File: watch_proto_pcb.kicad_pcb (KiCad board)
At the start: 2 copper layers, 32 parts, among them P1 CONN_01X04, P2 CONN_01X06, P3 CONN_01X04, Q1 RZM001P02, Q2 RZM001P02, Q3 RZM001P02, Q4 RZM001P02, U1 TLC5954

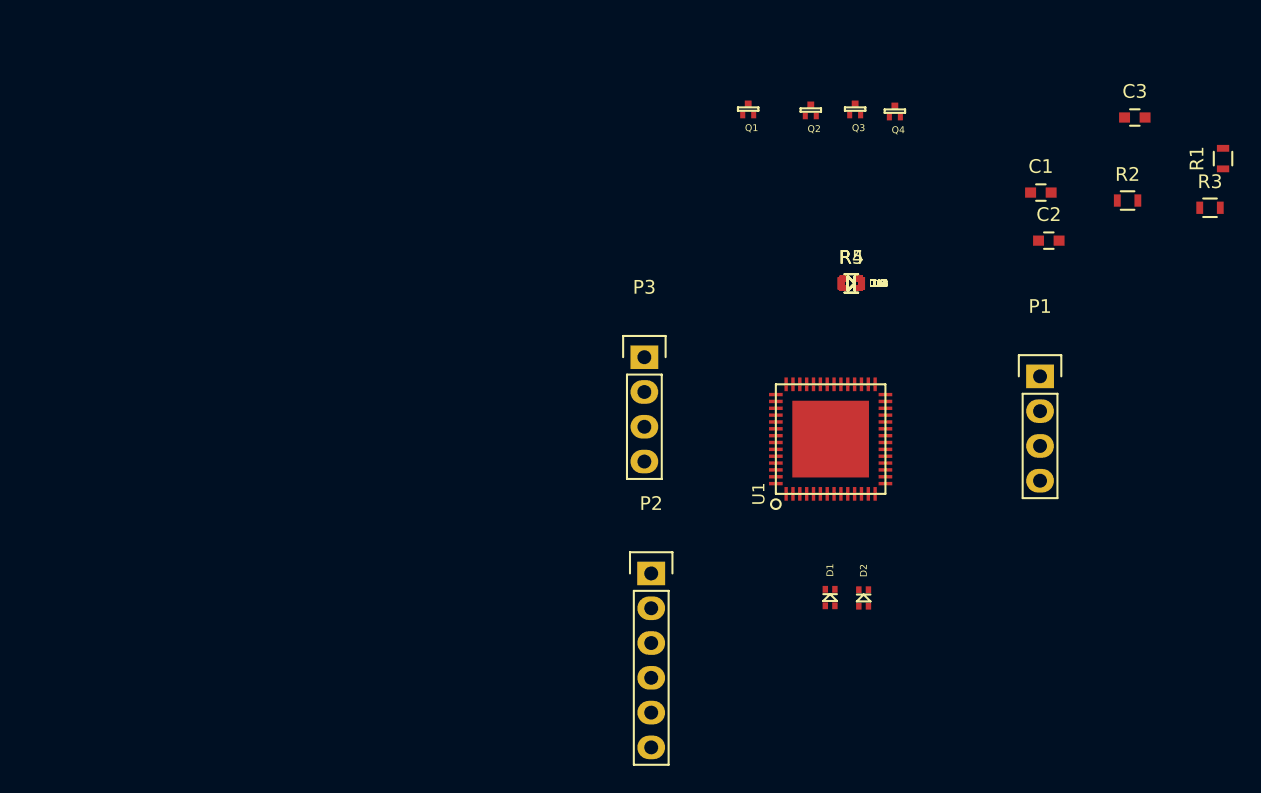
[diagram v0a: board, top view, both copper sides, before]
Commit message: Added debug messages and changed UI for rotation angle
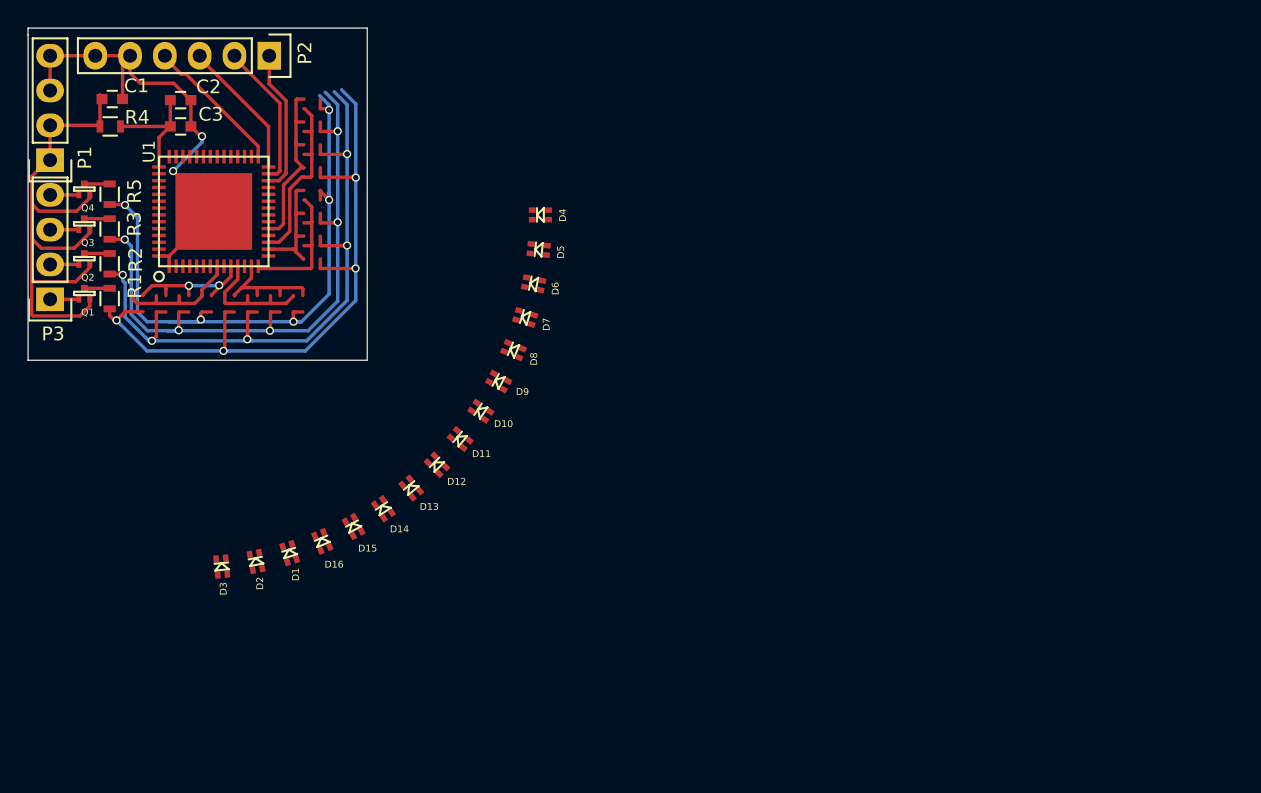
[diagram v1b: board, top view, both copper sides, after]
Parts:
- moved R1 81.9 mm to (94.3, 106.1), turned to 270 degrees
- moved R3 80.4 mm to (94.3, 101.0), turned to 270 degrees
- moved R2 74.5 mm to (94.3, 103.6), turned to 270 degrees
- moved P1 74.0 mm to (90.0, 96.0), turned to 180 degrees
- moved C3 69.7 mm to (99.5, 93.5)
- moved C1 68.1 mm to (94.5, 91.5)
- moved C2 64.2 mm to (99.5, 91.6)
- moved Q4 59.5 mm to (92.5, 97.7)
- moved Q3 56.9 mm to (92.5, 100.3)
- moved R4 55.3 mm to (94.4, 93.5), turned to 180 degrees
- moved R5 54.5 mm to (94.3, 98.5), turned to 270 degrees
- moved Q2 54.1 mm to (92.5, 102.8)
- moved D3 50.4 mm to (102.5, 125.7), turned to 95.625 degrees
- moved Q1 50.3 mm to (92.5, 105.4)
- moved U1 48.0 mm to (102.0, 99.8)
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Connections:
- C1 pad 1: /proto_TLC/TLC_PWR -> VDD
- C3 pad 1: VDD -> /proto_TLC/TLC_PWR
- D10 pad 1: /proto_TLC/B1 -> /proto_TLC/B2
- D10 pad 2: /proto_TLC/LED_PWR_OUT_0 -> /proto_TLC/LED_PWR_OUT_1
- D10 pad 3: /proto_TLC/R1 -> /proto_TLC/R2
- D10 pad 4: /proto_TLC/LED_PWR_OUT_0 -> /proto_TLC/LED_PWR_OUT_1
- D11 pad 1: /proto_TLC/B3 -> /proto_TLC/B2
- D11 pad 2: /proto_TLC/LED_PWR_OUT_1 -> /proto_TLC/LED_PWR_OUT_2
- D11 pad 3: /proto_TLC/R3 -> /proto_TLC/R2
- D11 pad 4: /proto_TLC/LED_PWR_OUT_1 -> /proto_TLC/LED_PWR_OUT_2
- D12 pad 1: /proto_TLC/B1 -> /proto_TLC/B2
- D12 pad 2: /proto_TLC/LED_PWR_OUT_1 -> /proto_TLC/LED_PWR_OUT_3
- D12 pad 3: /proto_TLC/R1 -> /proto_TLC/R2
- D12 pad 4: /proto_TLC/LED_PWR_OUT_1 -> /proto_TLC/LED_PWR_OUT_3
- D13 pad 2: /proto_TLC/LED_PWR_OUT_2 -> /proto_TLC/LED_PWR_OUT_0
- D13 pad 4: /proto_TLC/LED_PWR_OUT_2 -> /proto_TLC/LED_PWR_OUT_0
- D14 pad 1: /proto_TLC/B1 -> /proto_TLC/B3
- D14 pad 2: /proto_TLC/LED_PWR_OUT_2 -> /proto_TLC/LED_PWR_OUT_1
- D14 pad 3: /proto_TLC/R1 -> /proto_TLC/R3
- D14 pad 4: /proto_TLC/LED_PWR_OUT_2 -> /proto_TLC/LED_PWR_OUT_1
- D15 pad 2: /proto_TLC/LED_PWR_OUT_3 -> /proto_TLC/LED_PWR_OUT_2
- D15 pad 4: /proto_TLC/LED_PWR_OUT_3 -> /proto_TLC/LED_PWR_OUT_2
- D16 pad 1: /proto_TLC/B1 -> /proto_TLC/B3
- D16 pad 3: /proto_TLC/R1 -> /proto_TLC/R3
- D2 pad 1: /proto_TLC/B2 -> /proto_TLC/B0
- D2 pad 2: /proto_TLC/LED_PWR_OUT_0 -> /proto_TLC/LED_PWR_OUT_1
- D2 pad 3: /proto_TLC/R2 -> /proto_TLC/R0
- D2 pad 4: /proto_TLC/LED_PWR_OUT_0 -> /proto_TLC/LED_PWR_OUT_1
- D3 pad 2: /proto_TLC/LED_PWR_OUT_1 -> /proto_TLC/LED_PWR_OUT_2
- D3 pad 4: /proto_TLC/LED_PWR_OUT_1 -> /proto_TLC/LED_PWR_OUT_2
- D4 pad 1: /proto_TLC/B2 -> /proto_TLC/B0
- D4 pad 2: /proto_TLC/LED_PWR_OUT_1 -> /proto_TLC/LED_PWR_OUT_3
- D4 pad 3: /proto_TLC/R2 -> /proto_TLC/R0
- D4 pad 4: /proto_TLC/LED_PWR_OUT_1 -> /proto_TLC/LED_PWR_OUT_3
- D5 pad 1: /proto_TLC/B0 -> /proto_TLC/B1
- D5 pad 2: /proto_TLC/LED_PWR_OUT_2 -> /proto_TLC/LED_PWR_OUT_0
- D5 pad 3: /proto_TLC/R0 -> /proto_TLC/R1
- D5 pad 4: /proto_TLC/LED_PWR_OUT_2 -> /proto_TLC/LED_PWR_OUT_0
- D6 pad 1: /proto_TLC/B2 -> /proto_TLC/B1
- D6 pad 2: /proto_TLC/LED_PWR_OUT_2 -> /proto_TLC/LED_PWR_OUT_1
- D6 pad 3: /proto_TLC/R2 -> /proto_TLC/R1
- D6 pad 4: /proto_TLC/LED_PWR_OUT_2 -> /proto_TLC/LED_PWR_OUT_1
- D7 pad 1: /proto_TLC/B0 -> /proto_TLC/B1
- D7 pad 2: /proto_TLC/LED_PWR_OUT_3 -> /proto_TLC/LED_PWR_OUT_2
- D7 pad 3: /proto_TLC/R0 -> /proto_TLC/R1
- D7 pad 4: /proto_TLC/LED_PWR_OUT_3 -> /proto_TLC/LED_PWR_OUT_2
- D8 pad 1: /proto_TLC/B2 -> /proto_TLC/B1
- D8 pad 3: /proto_TLC/R2 -> /proto_TLC/R1
- D9 pad 1: /proto_TLC/B3 -> /proto_TLC/B2
- D9 pad 3: /proto_TLC/R3 -> Net-(D9-Pad3)
- R4 pad 1: /proto_TLC/LED_MOS_3 -> /proto_TLC/TLC_PWR
- R4 pad 2: /proto_TLC/LED_PWR_OUT_3 -> VDD
- R5 pad 1: /proto_TLC/TLC_PWR -> /proto_TLC/LED_MOS_3
- R5 pad 2: VDD -> /proto_TLC/LED_PWR_OUT_3
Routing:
- net /proto_TLC/LED_PWR_OUT_1: track 0.00 -> 49.4 mm, vias 0 -> 5
- net /proto_TLC/LED_PWR_OUT_3: track 0.00 -> 48.4 mm, vias 0 -> 5
- net /proto_TLC/LED_PWR_OUT_2: track 0.00 -> 47.8 mm, vias 0 -> 5
- net /proto_TLC/LED_PWR_OUT_0: track 0.00 -> 46.0 mm, vias 0 -> 3
- net VDD: track 0.00 -> 42.5 mm
- net GND: track 0.00 -> 35.0 mm, vias 0 -> 2
- net /proto_TLC/R3: track 0.00 -> 13.4 mm
- net /proto_TLC/B3: track 0.00 -> 13.2 mm
- net /proto_TLC/LAT: track 0.00 -> 10.7 mm
- net /proto_TLC/SIN: track 0.00 -> 10.6 mm
- net /proto_TLC/BLANK: track 0.00 -> 10.4 mm
- net /proto_TLC/R2: track 0.00 -> 10.4 mm
- net /proto_TLC/SCLK: track 0.00 -> 10.2 mm
- net /proto_TLC/B0: track 0.00 -> 10.2 mm, vias 0 -> 2
- net /proto_TLC/R1: track 0.00 -> 9.57 mm
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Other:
- board outline added: 24.8 x 24.3 mm
- net class small added: clearance 0.2, trace_width 0.2032, via_dia 7.62, via_drill 3.81

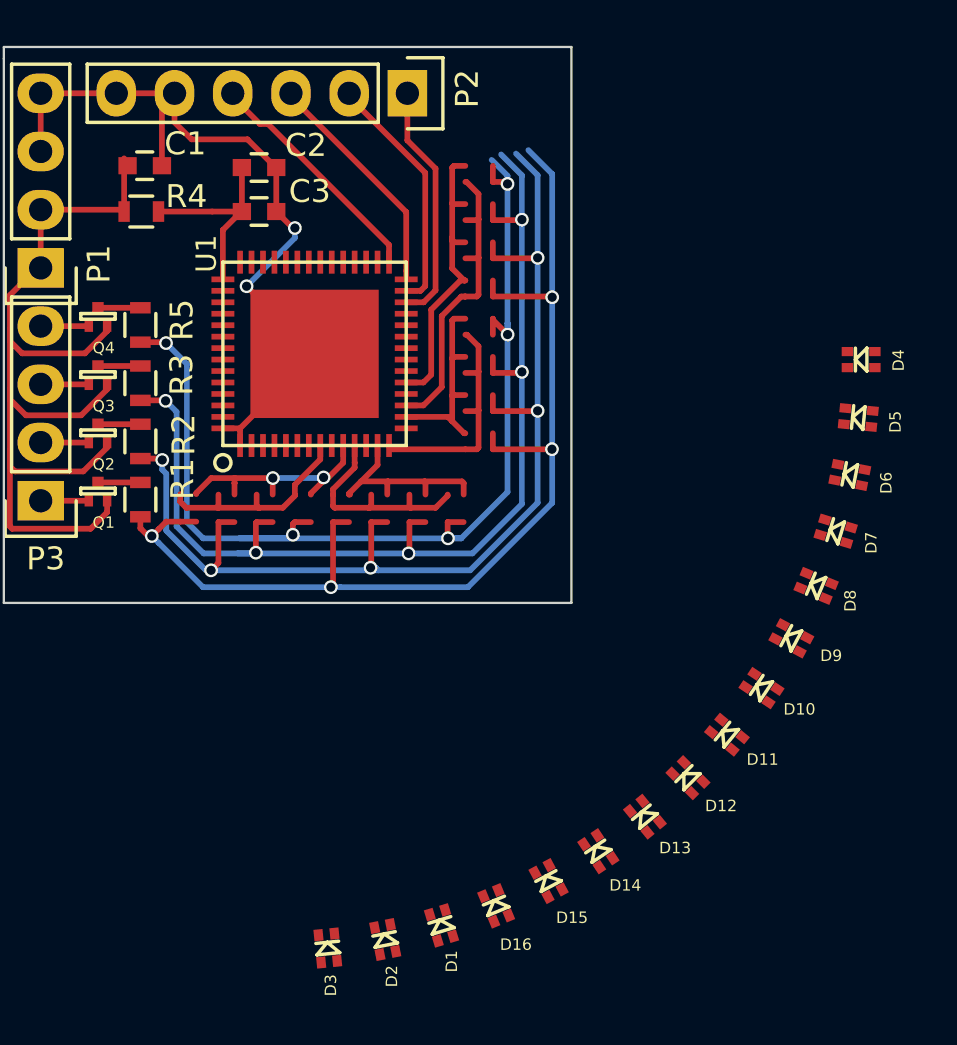
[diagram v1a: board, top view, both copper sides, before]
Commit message: Fixed double the radius issue
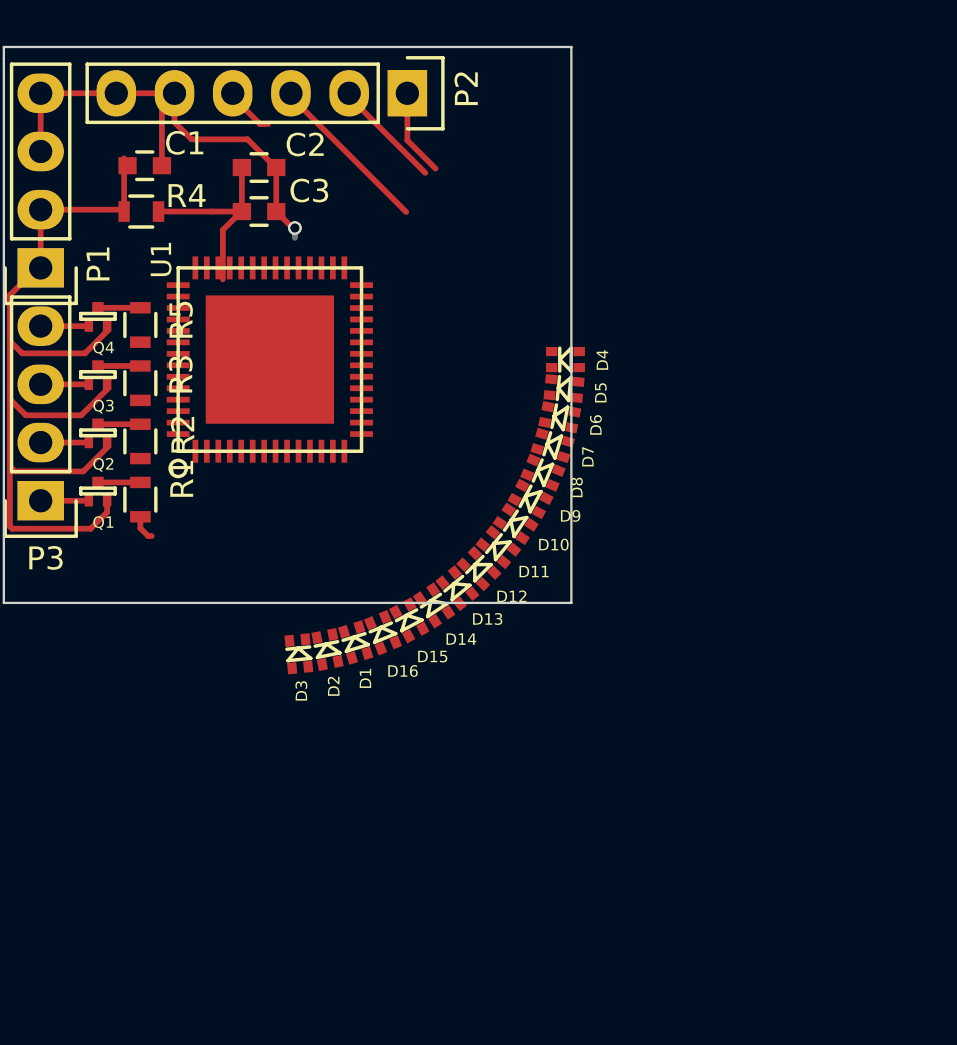
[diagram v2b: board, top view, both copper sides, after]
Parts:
- moved D10 12.9 mm to (110.7, 107.2)
- moved D14 12.9 mm to (107.2, 110.7)
- moved D4 12.9 mm to (112.9, 100.0)
- moved D15 12.9 mm to (106.1, 111.4)
- moved D9 12.9 mm to (111.4, 106.1)
- moved D3 12.9 mm to (101.3, 112.8)
- moved D5 12.9 mm to (112.8, 101.3)
- moved D2 12.9 mm to (102.5, 112.7)
- moved D6 12.9 mm to (112.7, 102.5)
- moved D16 12.9 mm to (104.9, 111.9)
- moved D8 12.9 mm to (111.9, 104.9)
- moved D1 12.9 mm to (103.7, 112.3)
- moved D7 12.9 mm to (112.3, 103.7)
- moved D11 12.9 mm to (110.0, 108.2)
- moved D13 12.9 mm to (108.2, 110.0)
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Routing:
- net /proto_TLC/LED_PWR_OUT_1: track 49.4 -> 0.00 mm, vias 5 -> 0
- net /proto_TLC/LED_PWR_OUT_3: track 48.4 -> 0.00 mm, vias 5 -> 0
- net /proto_TLC/LED_PWR_OUT_2: track 47.8 -> 0.00 mm, vias 5 -> 0
- net /proto_TLC/LED_PWR_OUT_0: track 46.0 -> 1.14 mm, vias 3 -> 0
- net /proto_TLC/R3: track 13.4 -> 0.00 mm
- net GND: track 35.0 -> 21.8 mm, vias 2 -> 1
- net /proto_TLC/B3: track 13.2 -> 0.00 mm
- net /proto_TLC/R2: track 10.4 -> 0.00 mm
- net /proto_TLC/B0: track 10.2 -> 0.00 mm, vias 2 -> 0
- net /proto_TLC/R1: track 9.57 -> 0.00 mm
- net /proto_TLC/R0: track 9.54 -> 0.00 mm
- net /proto_TLC/B2: track 9.07 -> 0.00 mm
- net /proto_TLC/B1: track 8.88 -> 0.00 mm
- net /proto_TLC/BLANK: track 10.4 -> 2.19 mm
- net /proto_TLC/SIN: track 10.6 -> 3.80 mm
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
